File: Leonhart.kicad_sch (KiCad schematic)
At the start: 0 parts

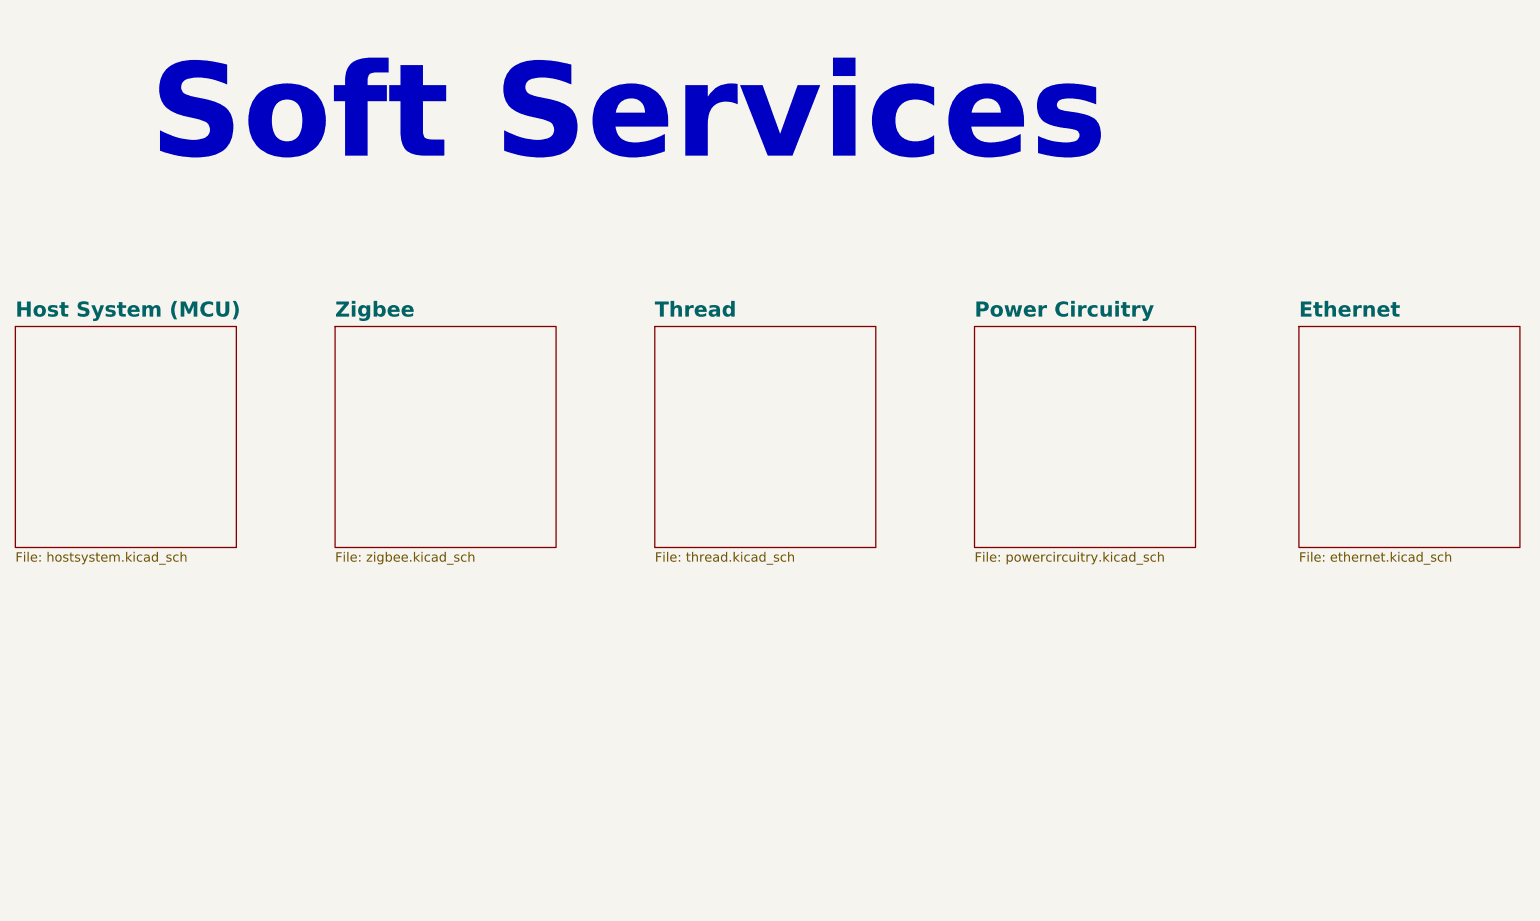
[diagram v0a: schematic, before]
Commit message: Started power circuitry and added more custom schematic symbols
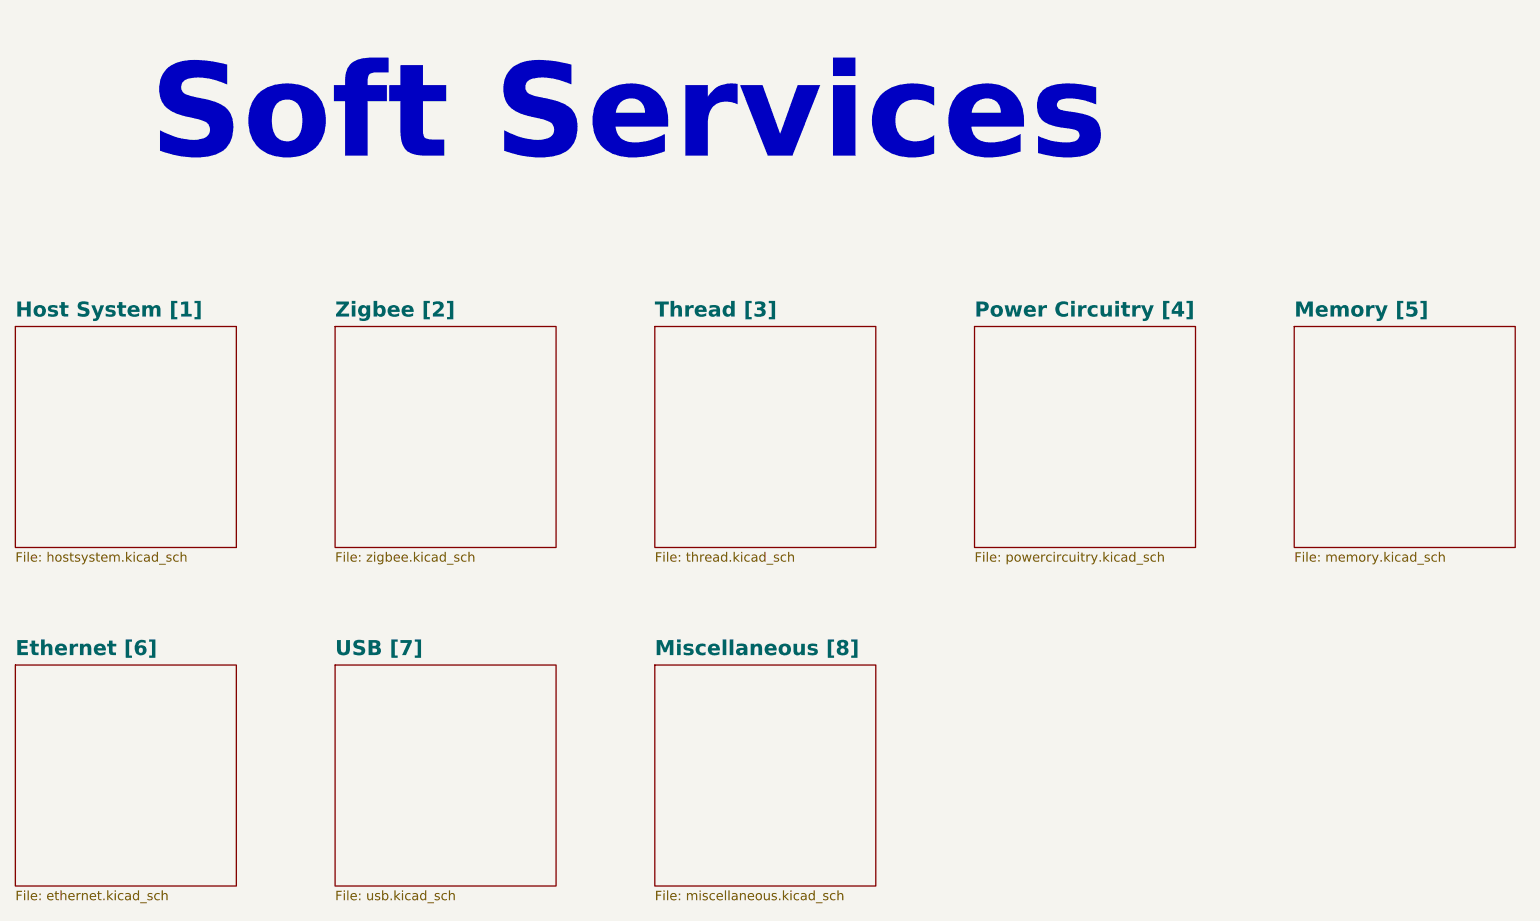
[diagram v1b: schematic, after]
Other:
- sheet Ethernet renamed Ethernet [6]
- sheet Host System (MCU) renamed Host System [1]
- sheet Power Circuitry renamed Power Circuitry [4]
- sheet Thread renamed Thread [3]
- sheet Zigbee renamed Zigbee [2]
- added sheet Memory [5] (memory.kicad_sch)
- added sheet Miscellaneous [8] (miscellaneous.kicad_sch)
- added sheet USB [7] (usb.kicad_sch)
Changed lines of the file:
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@@
+	)
+	(sheet
+		(at 210.82 63.5)
+		(size 29.845 29.845)
+		(exclude_from_sim no)
+		(in_bom yes)
+		(on_board yes)
+		(dnp no)
+		(fields_autoplaced yes)
+		(stroke
+			(width 0.1524)
+			(type solid)
+		)
+		(fill
+			(color 0 0 0 0.0000)
+		)
+		(property "Sheetname" "Memory [5]"
+			(at 210.82 62.4074 0)
+			(effects
+				(font
+					(size 2.032 2.032)
+					(thickness 0.4064)
+					(bold yes)
+				)
+				(justify left bottom)
+			)
+		)
+		(property "Sheetfile" "memory.kicad_sch"
+			(at 210.82 93.9296 0)
+			(effects
+				(font
+					(size 1.27 1.27)
+				)
+				(justify left top)
+			)
+		)
+		(instances
+			(project "Leonhart"
+				(path "/b43b7bca-e50d-42ec-8ff0-e0016dfefe0a"
+					(page "8")
+				)
+			)
+		)
 	)
 	(sheet
@@
 			(color 0 0 0 0.0000)
 		)
-		(property "Sheetname" "Power Circuitry"
+		(property "Sheetname" "Power Circuitry [4]"
 			(at 167.64 62.4074 0)
 			(effects
@@
 			(color 0 0 0 0.0000)
 		)
-		(property "Sheetname" "Zigbee"
+		(property "Sheetname" "Zigbee [2]"
 			(at 81.28 62.4074 0)
 			(effects
@@
 			(color 0 0 0 0.0000)
 		)
-		(property "Sheetname" "Host System (MCU)"
+		(property "Sheetname" "Host System [1]"
 			(at 38.1 62.4074 0)
 			(effects
@@
 	)
 	(sheet
-		(at 211.455 63.5)
-		(size 29.845 29.845)
-		(exclude_from_sim no)
-		(in_bom yes)
-		(on_board yes)
-		(dnp no)
-		(fields_autoplaced yes)
-		(stroke
-			(width 0.1524)
-			(type solid)
-		)
-		(fill
-			(color 0 0 0 0.0000)
-		)
-		(property "Sheetname" "Ethernet"
-			(at 211.455 62.4074 0)
+		(at 124.46 109.22)
+		(size 29.845 29.845)
+		(exclude_from_sim no)
+		(in_bom yes)
+		(on_board yes)
+		(dnp no)
+		(fields_autoplaced yes)
+		(stroke
+			(width 0.1524)
+			(type solid)
+		)
+		(fill
+			(color 0 0 0 0.0000)
+		)
+		(property "Sheetname" "Miscellaneous [8]"
+			(at 124.46 108.1274 0)
+			(effects
+				(font
+					(size 2.032 2.032)
+					(thickness 0.4064)
+					(bold yes)
+				)
+				(justify left bottom)
+			)
+		)
+		(property "Sheetfile" "miscellaneous.kicad_sch"
+			(at 124.46 139.6496 0)
+			(effects
+				(font
+					(size 1.27 1.27)
+				)
+				(justify left top)
+			)
+		)
+		(instances
+			(project "Leonhart"
+				(path "/b43b7bca-e50d-42ec-8ff0-e0016dfefe0a"
+					(page "9")
+				)
+			)
+		)
+	)
+	(sheet
+		(at 38.1 109.22)
+		(size 29.845 29.845)
+		(exclude_from_sim no)
+		(in_bom yes)
+		(on_board yes)
+		(dnp no)
+		(fields_autoplaced yes)
+		(stroke
+			(width 0.1524)
+			(type solid)
+		)
+		(fill
+			(color 0 0 0 0.0000)
+		)
+		(property "Sheetname" "Ethernet [6]"
+			(at 38.1 108.1274 0)
 			(effects
 				(font
@@
 		)
 		(property "Sheetfile" "ethernet.kicad_sch"
-			(at 211.455 93.9296 0)
+			(at 38.1 139.6496 0)
 			(effects
 				(font
@@
 			(color 0 0 0 0.0000)
 		)
-		(property "Sheetname" "Thread"
+		(property "Sheetname" "Thread [3]"
 			(at 124.46 62.4074 0)
 			(effects
@@
 				)
 			)
+		)
+	)
+	(sheet
+		(at 81.28 109.22)
+		(size 29.845 29.845)
+		(exclude_from_sim no)
+		(in_bom yes)
+		(on_board yes)
+		(dnp no)
+		(fields_autoplaced yes)
+		(stroke
+			(width 0.1524)
+			(type solid)
+		)
+		(fill
+			(color 0 0 0 0.0000)
+		)
+		(property "Sheetname" "USB [7]"
+			(at 81.28 108.1274 0)
+			(effects
+				(font
+					(size 2.032 2.032)
+					(thickness 0.4064)
+					(bold yes)
+				)
+				(justify left bottom)
+			)
+		)
+		(property "Sheetfile" "usb.kicad_sch"
+			(at 81.28 139.6496 0)
+			(effects
+				(font
+					(size 1.27 1.27)
+				)
+				(justify left top)
+			)
+		)
+		(instances
+			(project "Leonhart"
+				(path "/b43b7bca-e50d-42ec-8ff0-e0016dfefe0a"
+					(page "7")
+				)
+			)

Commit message: Added micro SD card circuitry
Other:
- sheet USB [7] renamed USB and SD [7]
- sheet USB and SD [7]: file usb.kicad_sch -> usb_and_sd.kicad_sch
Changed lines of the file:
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@@
 			(color 0 0 0 0.0000)
 		)
-		(property "Sheetname" "USB [7]"
+		(property "Sheetname" "USB and SD [7]"
 			(at 81.28 108.1274 0)
 			(effects
@@
 			)
 		)
-		(property "Sheetfile" "usb.kicad_sch"
+		(property "Sheetfile" "usb_and_sd.kicad_sch"
 			(at 81.28 139.6496 0)
 			(effects

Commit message: Switched out CC2652P and nRF52840 for MGM240P to run Zigbee and Thread
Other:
- added sheet Zigbee+Thread (Multi_Protocol_Radio.kicad_sch)
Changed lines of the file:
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@@
+	)
+	(sheet
+		(at 167.64 109.22)
+		(size 29.845 29.845)
+		(exclude_from_sim no)
+		(in_bom yes)
+		(on_board yes)
+		(dnp no)
+		(fields_autoplaced yes)
+		(stroke
+			(width 0.1524)
+			(type solid)
+		)
+		(fill
+			(color 0 0 0 0.0000)
+		)
+		(property "Sheetname" "Zigbee+Thread"
+			(at 167.64 108.1274 0)
+			(effects
+				(font
+					(size 2.032 2.032)
+					(thickness 0.4064)
+					(bold yes)
+				)
+				(justify left bottom)
+			)
+		)
+		(property "Sheetfile" "Multi_Protocol_Radio.kicad_sch"
+			(at 167.64 139.6496 0)
+			(effects
+				(font
+					(size 1.27 1.27)
+				)
+				(justify left top)
+			)
+		)
+		(instances
+			(project "Leonhart"
+				(path "/b43b7bca-e50d-42ec-8ff0-e0016dfefe0a"
+					(page "9")
+				)
+			)
+		)
 	)
 	(sheet
